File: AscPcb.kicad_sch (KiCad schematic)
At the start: 92 parts, among them J1 12402012E212A, J10 Conn_01x02_Pin, J11 Conn_01x02_Pin, J12 Conn_01x02_Pin, J13 Conn_01x02_Pin, J14 Conn_01x02_Pin, J15 Conn_01x02_Pin, J16 Conn_01x02_Pin, J17 Conn_01x02_Pin, J2 B2B-PH-K-S(LF)(SN)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

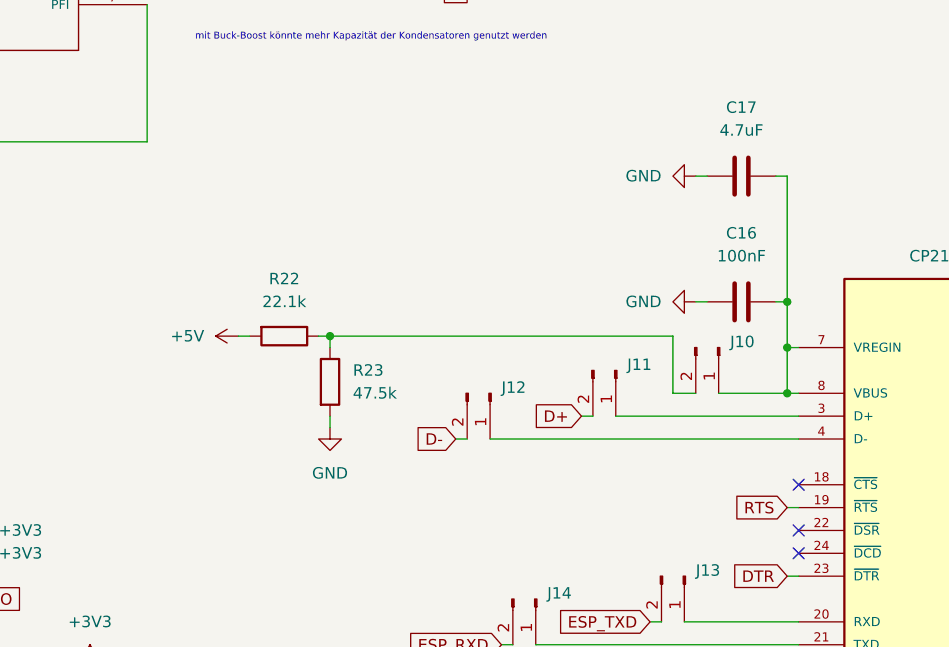
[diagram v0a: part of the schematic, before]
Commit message: started with pcb layout, did usb-c, buck, linear reg, bq24, cp2102
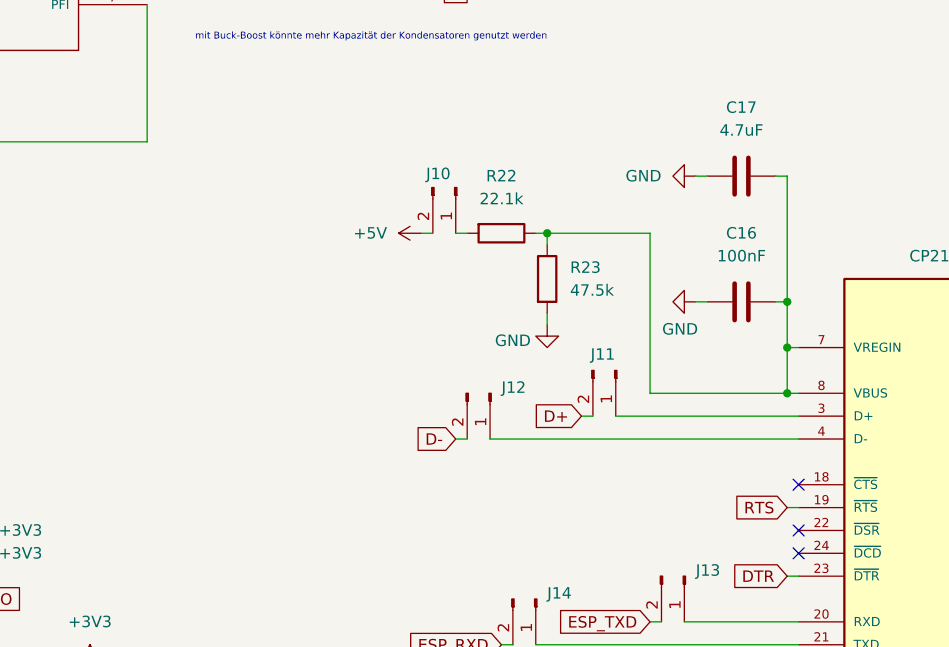
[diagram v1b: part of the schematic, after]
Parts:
- J5: footprint (none) -> Connector_PinHeader_2.54mm:PinHeader_1x15_P2.54mm_Vertical
- R11: footprint Resistor_SMD:R_0805_2012Metric -> Resistor_SMD:R_0603_1608Metric
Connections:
- net +5V: now also J10.2 (Pin_2); no longer R22.2
- net at C16.2, C17.2, U6.7 (VREGIN)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: now also R22.1, R23.1; no longer J10.1 (Pin_1)
- new net: J10.1 (Pin_1), R22.2
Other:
- moved on the sheet: J10, R22, R23
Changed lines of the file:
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@@
 	)
 	(junction
-		(at 123.19 198.12)
+		(at 147.32 186.69)
 		(diameter 0)
 		(color 0 0 0 0)
@@
 	(wire
 		(pts
-			(xy 161.29 204.47) (xy 163.83 204.47)
+			(xy 158.75 204.47) (xy 173.99 204.47)
 		)
 		(stroke
@@
 	(wire
 		(pts
-			(xy 166.37 204.47) (xy 173.99 204.47)
-		)
-		(stroke
-			(width 0)
-			(type default)
-		)
-	)
-	(wire
-		(pts
 			(xy 203.2 251.46) (xy 203.2 265.43)
 		)
@@
 	(wire
 		(pts
-			(xy 114.3 198.12) (xy 113.03 198.12)
-		)
-		(stroke
-			(width 0)
-			(type default)
-		)
-	)
-	(wire
-		(pts
 			(xy 204.47 251.46) (xy 203.2 251.46)
 		)
@@
 	(wire
 		(pts
-			(xy 161.29 204.47) (xy 161.29 198.12)
+			(xy 158.75 204.47) (xy 158.75 186.69)
 		)
 		(stroke
@@
 	(wire
 		(pts
-			(xy 121.92 198.12) (xy 123.19 198.12)
+			(xy 146.05 186.69) (xy 147.32 186.69)
 		)
 		(stroke
@@
 	(wire
 		(pts
-			(xy 161.29 198.12) (xy 123.19 198.12)
+			(xy 158.75 186.69) (xy 147.32 186.69)
 		)
 		(stroke
@@
 	(wire
 		(pts
+			(xy 133.35 186.69) (xy 134.62 186.69)
+		)
+		(stroke
+			(width 0)
+			(type default)
+		)
+	)
+	(wire
+		(pts
 			(xy 381 49.53) (xy 382.27 49.53)
 		)
@@
 	(wire
 		(pts
+			(xy 137.16 186.69) (xy 138.43 186.69)
+		)
+		(stroke
+			(width 0)
+			(type default)
+		)
+	)
+	(wire
+		(pts
 			(xy 127 142.24) (xy 127 140.97)
 		)
@@
 	(wire
 		(pts
-			(xy 123.19 198.12) (xy 123.19 199.39)
+			(xy 147.32 186.69) (xy 147.32 187.96)
 		)
 		(stroke
@@
 	(wire
 		(pts
-			(xy 123.19 208.28) (xy 123.19 207.01)
+			(xy 147.32 196.85) (xy 147.32 195.58)
 		)
 		(stroke
@@
 			)
 		)
-		(property "Footprint" ""
+		(property "Footprint" "Connector_PinHeader_2.54mm:PinHeader_1x15_P2.54mm_Vertical"
 			(at 387.35 67.31 0)
 			(effects
@@
 	(symbol
 		(lib_id "Device:R")
-		(at 118.11 198.12 270)
+		(at 142.24 186.69 270)
 		(unit 1)
 		(exclude_from_sim no)
@@
 		(fields_autoplaced yes)
 		(property "Reference" "R22"
-			(at 118.11 191.77 90)
+			(at 142.24 180.34 90)
 			(effects
 				(font
@@
 		)
 		(property "Value" "22.1k"
-			(at 118.11 194.31 90)
+			(at 142.24 182.88 90)
 			(effects
 				(font
@@
 		)
 		(property "Footprint" "Resistor_SMD:R_0603_1608Metric"
-			(at 118.11 196.342 90)
+			(at 142.24 184.912 90)
 			(effects
 				(font
@@
 		)
 		(property "Datasheet" "https://www.vishay.com/docs/20035/dcrcwe3.pdf"
-			(at 118.11 198.12 0)
+			(at 142.24 186.69 0)
 			(effects
 				(font
@@
 		)
 		(property "Description" "Resistor"
-			(at 118.11 198.12 0)
+			(at 142.24 186.69 0)
 			(effects
 				(font
@@
 		)
 		(property "MPN" "CRCW060322K1FKEA"
-			(at 118.11 198.12 0)
+			(at 142.24 186.69 0)
 			(effects
 				(font
@@
 		(on_board yes)
 		(dnp no)
-		(fields_autoplaced yes)
 		(property "Reference" "#PWR059"
 			(at 157.48 194.31 0)
@@
 		)
 		(property "Value" "GND"
-			(at 160.02 194.3099 90)
+			(at 164.084 197.358 90)
 			(effects
 				(font
@@
 	(symbol
 		(lib_id "power:GND")
-		(at 123.19 208.28 0)
+		(at 147.32 196.85 0)
 		(mirror y)
 		(unit 1)
@@
 		(on_board yes)
 		(dnp no)
-		(fields_autoplaced yes)
 		(property "Reference" "#PWR071"
-			(at 123.19 214.63 0)
+			(at 147.32 203.2 0)
 			(effects
 				(font
@@
 		)
 		(property "Value" "GND"
-			(at 123.19 213.36 0)
+			(at 143.51 198.628 0)
 			(effects
 				(font
@@
 		)
 		(property "Footprint" ""
-			(at 123.19 208.28 0)
+			(at 147.32 196.85 0)
 			(effects
 				(font
@@
 		)
 		(property "Datasheet" ""
-			(at 123.19 208.28 0)
+			(at 147.32 196.85 0)
 			(effects
 				(font
@@
 		)
 		(property "Description" "Power symbol creates a global label with name \"GND\" , ground"
-			(at 123.19 208.28 0)
+			(at 147.32 196.85 0)
 			(effects
 				(font
@@
 	(symbol
 		(lib_id "power:+5V")
-		(at 113.03 198.12 90)
+		(at 133.35 186.69 90)
 		(unit 1)
 		(exclude_from_sim no)
@@
 		(fields_autoplaced yes)
 		(property "Reference" "#PWR070"
-			(at 116.84 198.12 0)
+			(at 137.16 186.69 0)
 			(effects
 				(font
@@
 		)
 		(property "Value" "+5V"
-			(at 109.22 198.1199 90)
+			(at 129.54 186.6899 90)
 			(effects
 				(font
@@
 		)
 		(property "Footprint" ""
-			(at 113.03 198.12 0)
+			(at 133.35 186.69 0)
 			(effects
 				(font
@@
 		)
 		(property "Datasheet" ""
-			(at 113.03 198.12 0)
+			(at 133.35 186.69 0)
 			(effects
 				(font
@@
 		)
 		(property "Description" "Power symbol creates a global label with name \"+5V\""
-			(at 113.03 198.12 0)
+			(at 133.35 186.69 0)
 			(effects
 				(font
@@
 		(on_board yes)
 		(dnp no)
-		(fields_autoplaced yes)
 		(property "Reference" "J11"
-			(at 156.21 201.2949 90)
+			(at 152.146 200.152 90)
 			(effects
 				(font
@@
 	(symbol
 		(lib_id "Connector:Conn_01x02_Pin")
-		(at 166.37 199.39 270)
+		(at 137.16 181.61 270)
 		(unit 1)
 		(exclude_from_sim no)
@@
 		(on_board yes)
 		(dnp no)
-		(fields_autoplaced yes)
 		(property "Reference" "J10"
-			(at 167.64 198.7549 90)
+			(at 133.858 180.086 90)
 			(effects
 				(font
@@
 		)
 		(property "Value" "Conn_01x02_Pin"
-			(at 167.64 201.2949 90)
+			(at 138.43 183.5149 90)
 			(effects
 				(font
@@
 		)
 		(property "Footprint" "Connector_PinHeader_2.54mm:PinHeader_1x02_P2.54mm_Vertical"
-			(at 166.37 199.39 0)
+			(at 137.16 181.61 0)
 			(effects
 				(font
@@
 		)
 		(property "Datasheet" "~"
-			(at 166.37 199.39 0)
+			(at 137.16 181.61 0)
 			(effects
 				(font
@@
 		)
 		(property "Description" "Generic connector, single row, 01x02, script generated"
-			(at 166.37 199.39 0)
+			(at 137.16 181.61 0)
 			(effects
 				(font
@@
 	(symbol
 		(lib_id "Device:R")
-		(at 123.19 203.2 0)
+		(at 147.32 191.77 0)
 		(unit 1)
 		(exclude_from_sim no)
@@
 		(fields_autoplaced yes)
 		(property "Reference" "R23"
-			(at 125.73 201.9299 0)
+			(at 149.86 190.4999 0)
 			(effects
 				(font
@@
 		)
 		(property "Value" "47.5k"
-			(at 125.73 204.4699 0)
+			(at 149.86 193.0399 0)
 			(effects
 				(font
@@
 		)
 		(property "Footprint" "Resistor_SMD:R_0603_1608Metric"
-			(at 121.412 203.2 90)
+			(at 145.542 191.77 90)
 			(effects
 				(font
@@
 		)
 		(property "Datasheet" "https://www.vishay.com/docs/28773/crcwce3.pdf"
-			(at 123.19 203.2 0)
+			(at 147.32 191.77 0)
 			(effects
 				(font
@@
 		)
 		(property "Description" "Resistor"
-			(at 123.19 203.2 0)
+			(at 147.32 191.77 0)
 			(effects
 				(font
@@
 		)
 		(property "MPN" "CRCW060347K5FKEAC"
-			(at 123.19 203.2 0)
+			(at 147.32 191.77 0)
 			(effects
 				(font
@@
 		)
 		(property "Sim.Pins" ""
-			(at 123.19 203.2 90)
+			(at 147.32 191.77 90)
 			(effects
 				(font
@@
 			)
 		)
-		(property "Footprint" "Resistor_SMD:R_0805_2012Metric"
+		(property "Footprint" "Resistor_SMD:R_0603_1608Metric"
 			(at 92.202 91.44 90)
 			(effects

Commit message: first attempt at putting down traces
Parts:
- removed J11, J12, J13, J14: Conn_01x02_Pin, Connector_PinHeader_2.54mm:PinHeader_1x02_P2.54mm_Vertical, symbol Connector:Conn_01x02_Pin
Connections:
- net D+: now also U6.3 (D+)
- net D-: now also U6.4 (D-)
- net ESP_RXD: now also U6.21 (TXD)
- net ESP_TXD: now also U6.20 (RXD)

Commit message: routing done not gnd
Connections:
- net ESP_RXD: now also J5.14 (Pin_14); no longer J5.15 (Pin_15)
- net ESP_TXD: now also J5.15 (Pin_15); no longer J5.14 (Pin_14)
- net IO0: now also J5.13 (Pin_13); no longer J5.4 (Pin_4)
- net IO1: now also J5.12 (Pin_12); no longer J5.5 (Pin_5)
- net IO10: now also J5.6 (Pin_6); no longer J5.11 (Pin_11)
- net IO18: now also J5.5 (Pin_5); no longer J5.12 (Pin_12)
- net IO19: now also J5.4 (Pin_4); no longer J5.13 (Pin_13)
- net IO3: now also J5.11 (Pin_11); no longer J5.6 (Pin_6)
- net IO4: now also J5.10 (Pin_10); no longer J5.7 (Pin_7)
- net IO5: now also J5.9 (Pin_9); no longer J5.8 (Pin_8)
- net IO6: now also J5.8 (Pin_8); no longer J5.9 (Pin_9)
- net IO7: now also J5.7 (Pin_7); no longer J5.10 (Pin_10)
